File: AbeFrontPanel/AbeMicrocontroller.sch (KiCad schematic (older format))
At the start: 15 parts

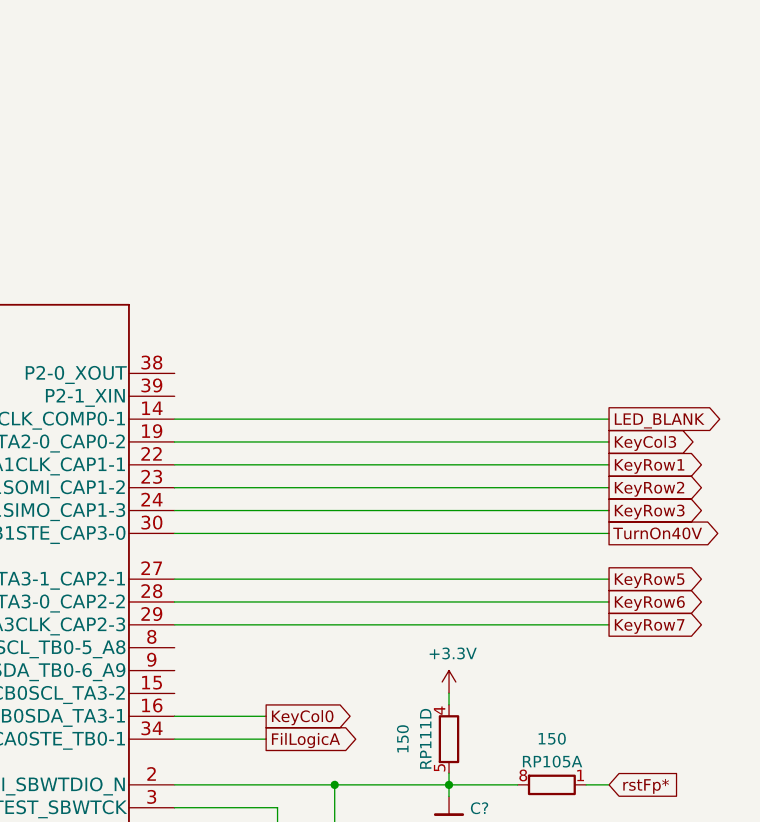
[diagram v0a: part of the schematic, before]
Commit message: +10V, Beeper
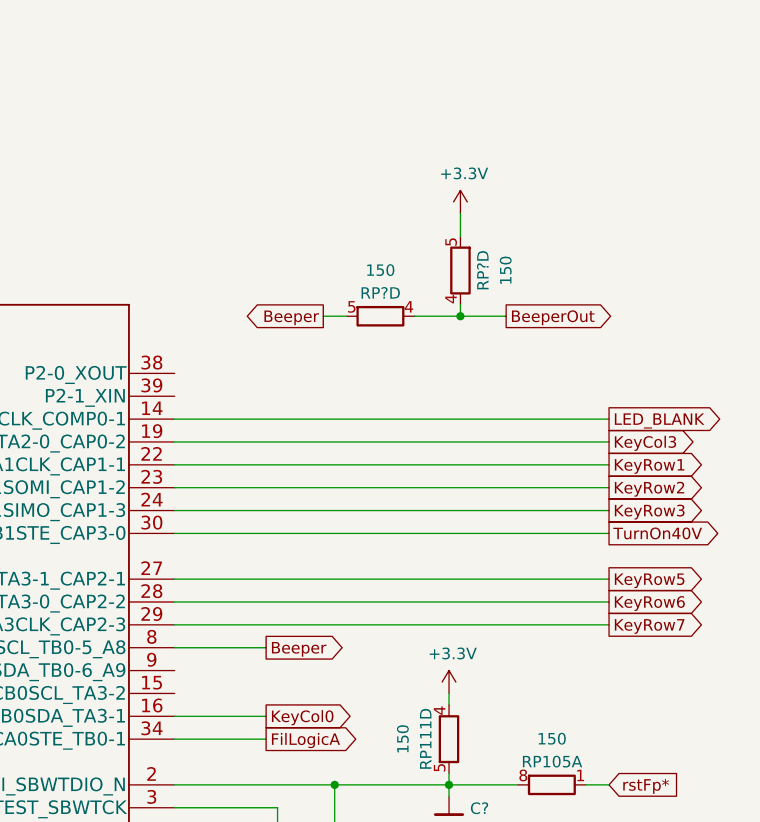
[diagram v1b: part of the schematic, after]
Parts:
- added RP? (x2): 150, symbol Device:R_Pack04_Split
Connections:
- net +3V3: now also RP?.5 (R4.2)
- net Beeper: now reaches U?.8 (P4-3_UCB1SOMI_UCB1SCL_TB0-5_A8)
- net Beeper: now also RP?.5 (R4.2)
- new net BeeperOut: RP?.4 (R4.1), RP?.4 (R4.1)
